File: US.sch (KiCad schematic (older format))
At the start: 1 part, among them J10 Conn_01x04

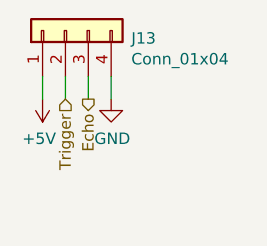
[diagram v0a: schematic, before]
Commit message: Added power selector for ultrasonic sensors
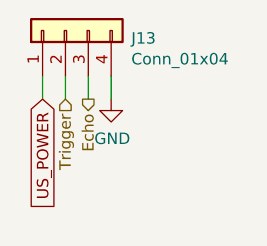
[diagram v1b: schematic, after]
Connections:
- net +5V renamed US_POWER
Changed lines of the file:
@@
-$EndComp
-$Comp
-L power:+5V #PWR043
-U 1 1 5BC0723E
-P 3900 2850
-AR Path="/5BC0526F/5BC0723E" Ref="#PWR043"  Part="1"
-AR Path="/5BC05277/5BC0723E" Ref="#PWR047"  Part="1"
-AR Path="/5BC05284/5BC0723E" Ref="#PWR051"  Part="1"
-AR Path="/5BC05291/5BC0723E" Ref="#PWR055"  Part="1"
-F 0 "#PWR055" H 3900 2700 50  0001 C CNN
-F 1 "+5V" H 3915 3023 50  0000 C CNN
-F 2 "" H 3900 2850 50  0001 C CNN
-F 3 "" H 3900 2850 50  0001 C CNN
-	1    3900 2850
-	-1   0    0    1
 $EndComp
 $Comp
@@
 Wire Wire Line
 	4100 2750 4100 2850
+Text GLabel 3900 2850 3    50   Input ~ 0
+US_POWER
 $EndSCHEMATC

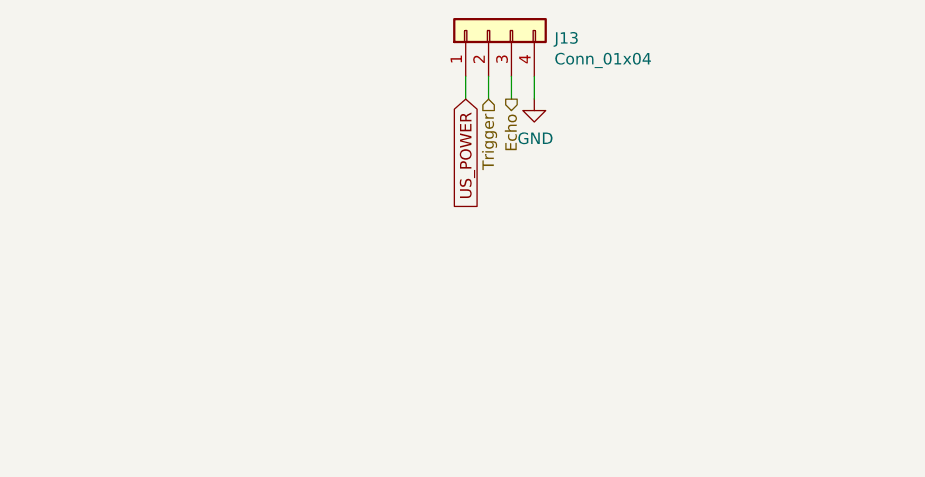
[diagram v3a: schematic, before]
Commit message: Fixed TTa pins issue
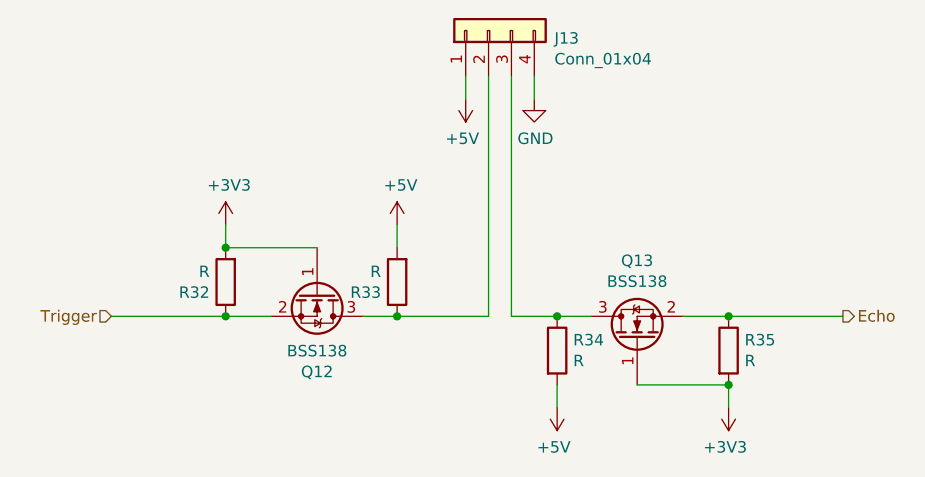
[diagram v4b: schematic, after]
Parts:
- added Q6, Q7: BSS138, Package_TO_SOT_SMD:SOT-23, symbol Transistor_FET:BSS138
- added R20, R21, R22, R23: R, symbol Device:R
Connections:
- net Echo: now also Q7.2 (S), R23.1; no longer J10.3 (Pin_3)
- net Trigger: now also Q6.2 (S), R20.1; no longer J10.2 (Pin_2)
- net US_POWER renamed +5V
- net +5V: now also R21.2, R22.2
- new net: J10.2 (Pin_2), Q6.3 (D), R21.1
- new net: J10.3 (Pin_3), Q7.3 (D), R22.1
- new net +3V3: Q6.1 (G), Q7.1 (G), R20.2, R23.2

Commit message: Added IC for level translation with ultrasonic sensors
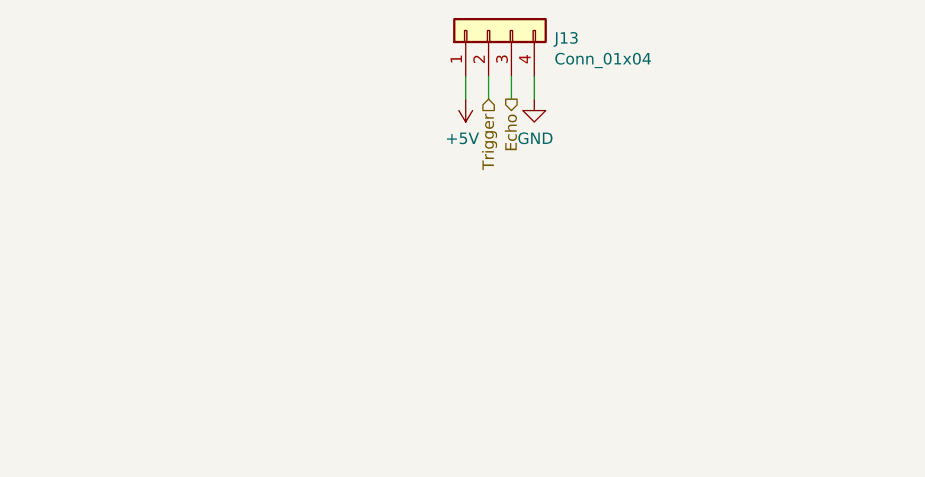
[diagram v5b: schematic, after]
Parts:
- removed Q6, Q7: BSS138, Package_TO_SOT_SMD:SOT-23, symbol Transistor_FET:BSS138
- removed R20, R21, R22, R23: R, symbol Device:R
- J10: footprint (none) -> Connector_JST:JST_XH_B04B-XH-A_1x04_P2.50mm_Vertical
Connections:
- net Echo: now also J10.3 (Pin_3)
- net Trigger: now also J10.2 (Pin_2)

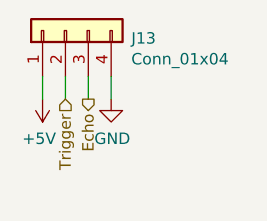
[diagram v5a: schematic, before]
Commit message: Added ultrasonic sensors power selection
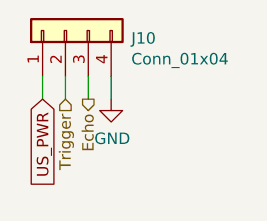
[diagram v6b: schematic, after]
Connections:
- net +5V renamed US_PWR
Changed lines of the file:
@@
 AR Path="/5BC05284/5BC053B5" Ref="J12"  Part="1"
 AR Path="/5BC05291/5BC053B5" Ref="J13"  Part="1"
-F 0 "J13" V 3966 2262 50  0000 R CNN
+F 0 "J10" V 3966 2262 50  0000 R CNN
 F 1 "Conn_01x04" V 3875 2262 50  0000 R CNN
 F 2 "Connector_JST:JST_XH_B04B-XH-A_1x04_P2.50mm_Vertical" H 4000 2550 50  0001 C CNN
@@
 AR Path="/5BC05284/5BC072A4" Ref="#PWR053"  Part="1"
 AR Path="/5BC05291/5BC072A4" Ref="#PWR055"  Part="1"
-F 0 "#PWR055" H 4200 2600 50  0001 C CNN
+F 0 "#PWR049" H 4200 2600 50  0001 C CNN
 F 1 "GND" H 4205 2677 50  0000 C CNN
 F 2 "" H 4200 2850 50  0001 C CNN
@@
 Text HLabel 4100 2850 3    50   Output ~ 0
 Echo
-$Comp
-L power:+5V #PWR048
-U 1 1 5BBF3C89
-P 3900 2850
-AR Path="/5BC0526F/5BBF3C89" Ref="#PWR048"  Part="1"
-AR Path="/5BC05277/5BBF3C89" Ref="#PWR050"  Part="1"
-AR Path="/5BC05284/5BBF3C89" Ref="#PWR052"  Part="1"
-AR Path="/5BC05291/5BBF3C89" Ref="#PWR054"  Part="1"
-F 0 "#PWR054" H 3900 2700 50  0001 C CNN
-F 1 "+5V" H 3915 3023 50  0000 C CNN
-F 2 "" H 3900 2850 50  0001 C CNN
-F 3 "" H 3900 2850 50  0001 C CNN
-	1    3900 2850
-	-1   0    0    1
-$EndComp
 Wire Wire Line
 	4000 2750 4000 2850
 Wire Wire Line
 	4100 2750 4100 2850
+Text GLabel 3900 2850 3    50   Input ~ 0
+US_PWR
 $EndSCHEMATC

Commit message: Footprint association
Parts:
- J10: footprint Connector_JST:JST_XH_B04B-XH-A_1x04_P2.50mm_Vertical -> Connector_JST:JST_PH_B4B-PH-K_1x04_P2.00mm_Vertical
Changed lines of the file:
@@
 F 0 "J10" V 3966 2262 50  0000 R CNN
 F 1 "Conn_01x04" V 3875 2262 50  0000 R CNN
-F 2 "Connector_JST:JST_XH_B04B-XH-A_1x04_P2.50mm_Vertical" H 4000 2550 50  0001 C CNN
+F 2 "Connector_JST:JST_PH_B4B-PH-K_1x04_P2.00mm_Vertical" H 4000 2550 50  0001 C CNN
 F 3 "~" H 4000 2550 50  0001 C CNN
 	1    4000 2550
@@
 AR Path="/5BC05284/5BC072A4" Ref="#PWR053"  Part="1"
 AR Path="/5BC05291/5BC072A4" Ref="#PWR055"  Part="1"
-F 0 "#PWR049" H 4200 2600 50  0001 C CNN
+F 0 "#PWR055" H 4200 2600 50  0001 C CNN
 F 1 "GND" H 4205 2677 50  0000 C CNN
 F 2 "" H 4200 2850 50  0001 C CNN

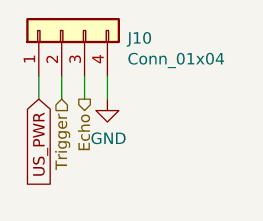
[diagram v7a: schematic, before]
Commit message: Schematic corrections
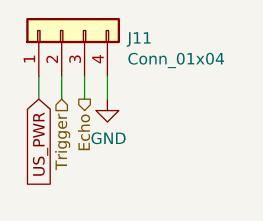
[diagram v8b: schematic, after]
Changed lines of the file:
@@
 AR Path="/5BC05284/5BC053B5" Ref="J12"  Part="1"
 AR Path="/5BC05291/5BC053B5" Ref="J13"  Part="1"
-F 0 "J10" V 3966 2262 50  0000 R CNN
+F 0 "J11" V 3966 2262 50  0000 R CNN
 F 1 "Conn_01x04" V 3875 2262 50  0000 R CNN
 F 2 "Connector_JST:JST_PH_B4B-PH-K_1x04_P2.00mm_Vertical" H 4000 2550 50  0001 C CNN
@@
 $EndComp
 $Comp
-L power:GND #PWR049
+L power:GND #PWR051
 U 1 1 5BC072A4
 P 4200 2850
-AR Path="/5BC0526F/5BC072A4" Ref="#PWR049"  Part="1"
-AR Path="/5BC05277/5BC072A4" Ref="#PWR051"  Part="1"
+AR Path="/5BC0526F/5BC072A4" Ref="#PWR051"  Part="1"
+AR Path="/5BC05277/5BC072A4" Ref="#PWR052"  Part="1"
 AR Path="/5BC05284/5BC072A4" Ref="#PWR053"  Part="1"
-AR Path="/5BC05291/5BC072A4" Ref="#PWR055"  Part="1"
-F 0 "#PWR055" H 4200 2600 50  0001 C CNN
+AR Path="/5BC05291/5BC072A4" Ref="#PWR054"  Part="1"
+F 0 "#PWR052" H 4200 2600 50  0001 C CNN
 F 1 "GND" H 4205 2677 50  0000 C CNN
 F 2 "" H 4200 2850 50  0001 C CNN
